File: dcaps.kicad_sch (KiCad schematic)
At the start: 1 part, among them U1 AM6254ATCGHAALW

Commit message: commit++
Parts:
- removed U1: AM6254ATCGHAALW, pepy_sym_lib:[CPU]Texas Instruments AM6254ATCGHAALW, symbol pepy_sym_lib:[CPU]Texas Instruments AM6254ATCGHAALW
- added C10, C11, C12, C13, C15, C16, C17, C8, C9: CL03A105MQ3CSNH, pepy_sym_lib:[CAP_SMD_0201_0603Metric], symbol pepy_sym_lib:[CAP_SMD_0201_0603Metric]Samsung Electro-Mechanics CL03A105MQ3CSNH
- added U1: AM6254ATCGHAALW, pepy_sym_lib:[CPU]Texas Instruments AM6254ATCGHAALW, symbol pepy_sym_lib:[CPU]Texas Instruments AM6254ATCGHAALW
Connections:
- new net: C9.2, U1.H11 (CAP_VDDS_MCU)
- new net: C15.2, U1.H15 (CAP_VDDS0)
- new net: C10.2, U1.J19 (CAP_VDDS6)
- new net: C17.2, U1.W17 (CAP_VDDS2)
- new net: C16.2, U1.K18 (CAP_VDDS1)
- new net: C12.2, U1.U7 (CAP_VDDS4)
- new net: C13.2, U1.H17 (CAP_VDDS5)
- new net: C8.2, U1.G9 (CAP_VDDS_CANUART)
- new net: C11.2, U1.P19 (CAP_VDDS3)
- new net GND: C10.1, C11.1, C12.1, C13.1, C15.1, C16.1, C17.1, C8.1, C9.1, U1.A1 (VSS), U1.A24 (VSS), U1.A25 (VSS), U1.AA11 (VSS), U1.AB9 (VSS), U1.AD1 (VSS), U1.AD12 (VSS), U1.AD16 (VSS), U1.AD25 (VSS), U1.AD9 (VSS), U1.AE1 (VSS), U1.AE12 (VSS), U1.AE16 (VSS), U1.AE24 (VSS), U1.AE25 (VSS), U1.AE8 (VSS), U1.B25 (VSS), U1.F13 (VSS), U1.G13 (VSS), U1.G19 (VSS), U1.H13 (VSS), U1.H16 (VSS), U1.H18 (VSS), U1.H20 (VSS), U1.J13 (VSS), U1.J7 (VSS), U1.K13 (VSS), U1.K15 (VSS), U1.K19 (VSS), U1.K7 (VSS), U1.L20 (VSS), U1.M10 (VSS), U1.M12 (VSS), U1.M13 (VSS), U1.M17 (VSS), U1.M18 (VSS), U1.M7 (VSS), U1.M8 (VSS), U1.N15 (VSS), U1.P10 (VSS), U1.P13 (VSS), U1.P7 (VSS), U1.R13 (VSS), U1.R15 (VSS), U1.R18 (VSS), U1.R20 (VSS), U1.T13 (VSS), U1.T14 (VSS), U1.T16 (VSS), U1.T17 (VSS), U1.T18 (VSS), U1.T8 (VSS), U1.U19 (VSS), U1.U8 (VSS), U1.V10 (VSS), U1.V11 (VSS), U1.V13 (VSS), U1.V16 (VSS), U1.V18 (VSS), U1.V9 (VSS), U1.W7 (VSS), U1.Y2 (VSS)

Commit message: PMIC draft
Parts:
- added C37: CL03A105MQ3CSNH, pepy_sym_lib:[CAP_SMD_0201_0603Metric], symbol pepy_sym_lib:[CAP_SMD_0201_0603Metric]Samsung Electro-Mechanics CL03A105MQ3CSNH
- added C38, C39, C40, C41, C42, C43, C44, C45, C46, C47, C48, C49, C50, C51, C52, C53: CC0201KRX5R6BB104, pepy_sym_lib:[CAP_SMD_0201_0603Metric], symbol pepy_sym_lib:[CAP_SMD_0201_0603Metric]YAGEO CC0201KRX5R6BB104
- added C54: CL05A475KP5NRNC, pepy_sym_lib:[CAP_SMD_0402_1005Metric], symbol pepy_sym_lib:[CAP_SMD_0402_1005Metric]Samsung Electro-Mechanics CL05A475KP5NRNC
- added C55: CC0402MRX5R5BB106, pepy_sym_lib:[CAP_SMD_0402_1005Metric], symbol pepy_sym_lib:[CAP_SMD_0402_1005Metric]YAGEO CC0402MRX5R5BB106
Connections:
- net GND: now also C37.1, C38.1, C39.1, C40.1, C41.1, C42.1, C43.1, C44.1, C45.1, C46.1, C47.1, C48.1, C49.1, C50.1, C51.1, C52.1, C53.1, C54.1, C55.1
- new net VDD_CORE: C37.2, C38.2, C39.2, C40.2, C41.2, C42.2, C43.2, C44.2, C45.2, C46.2, C47.2, C48.2, C49.2, C50.2, C51.2, C52.2, C53.2, C54.2, C55.2

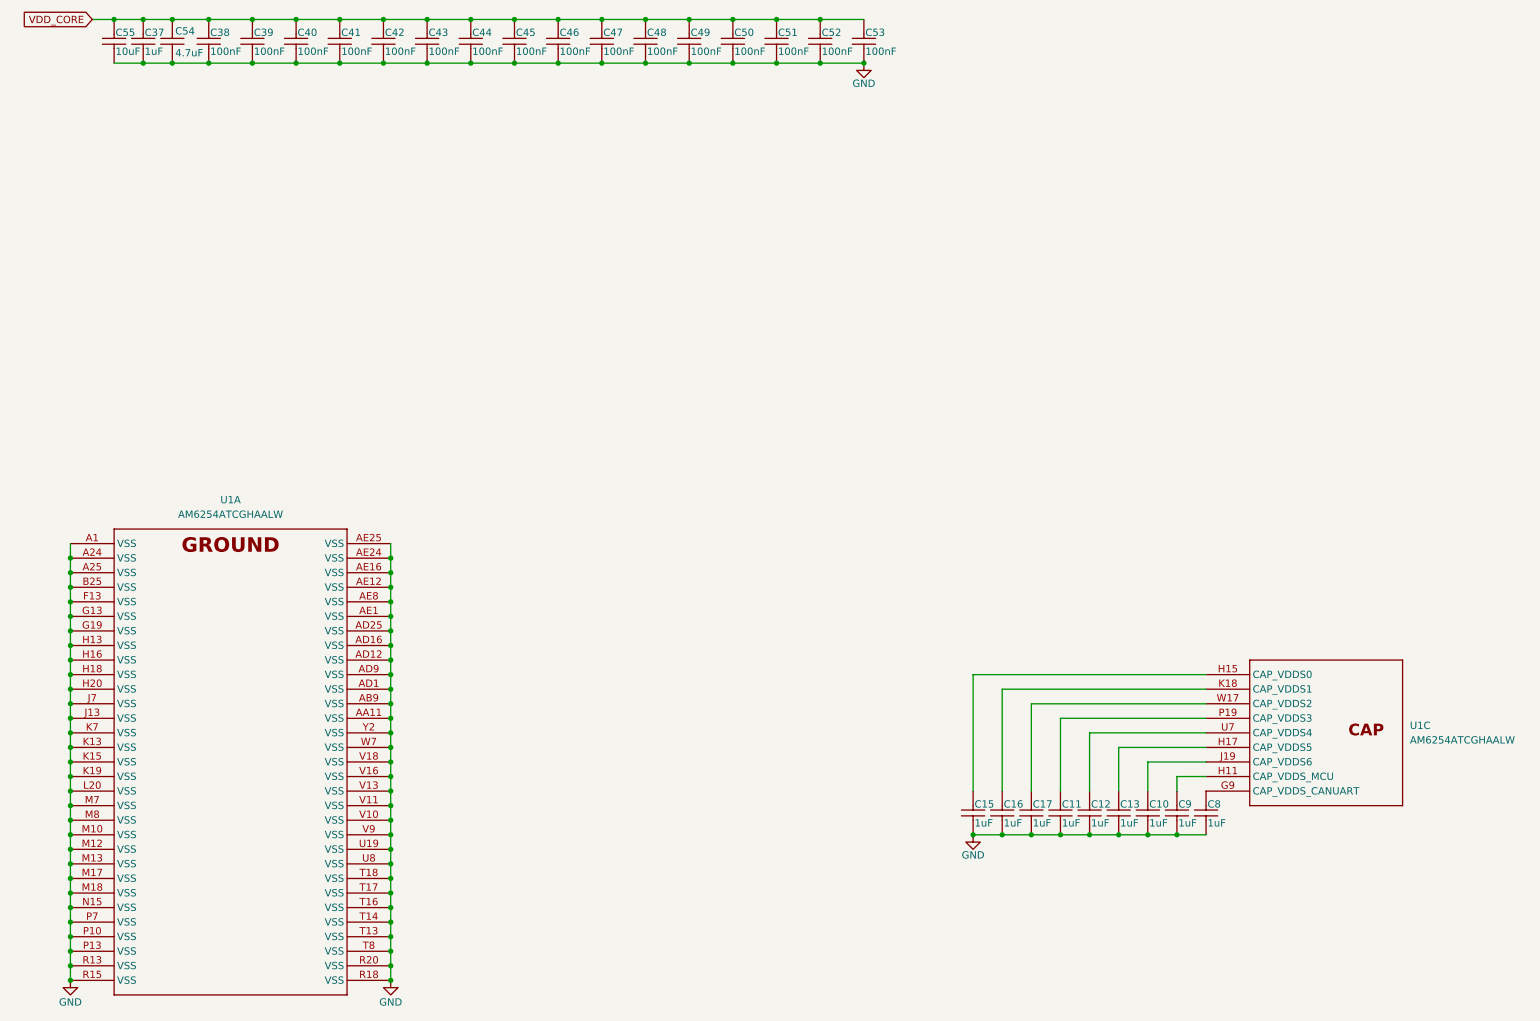
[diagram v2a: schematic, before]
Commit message: SD card changes
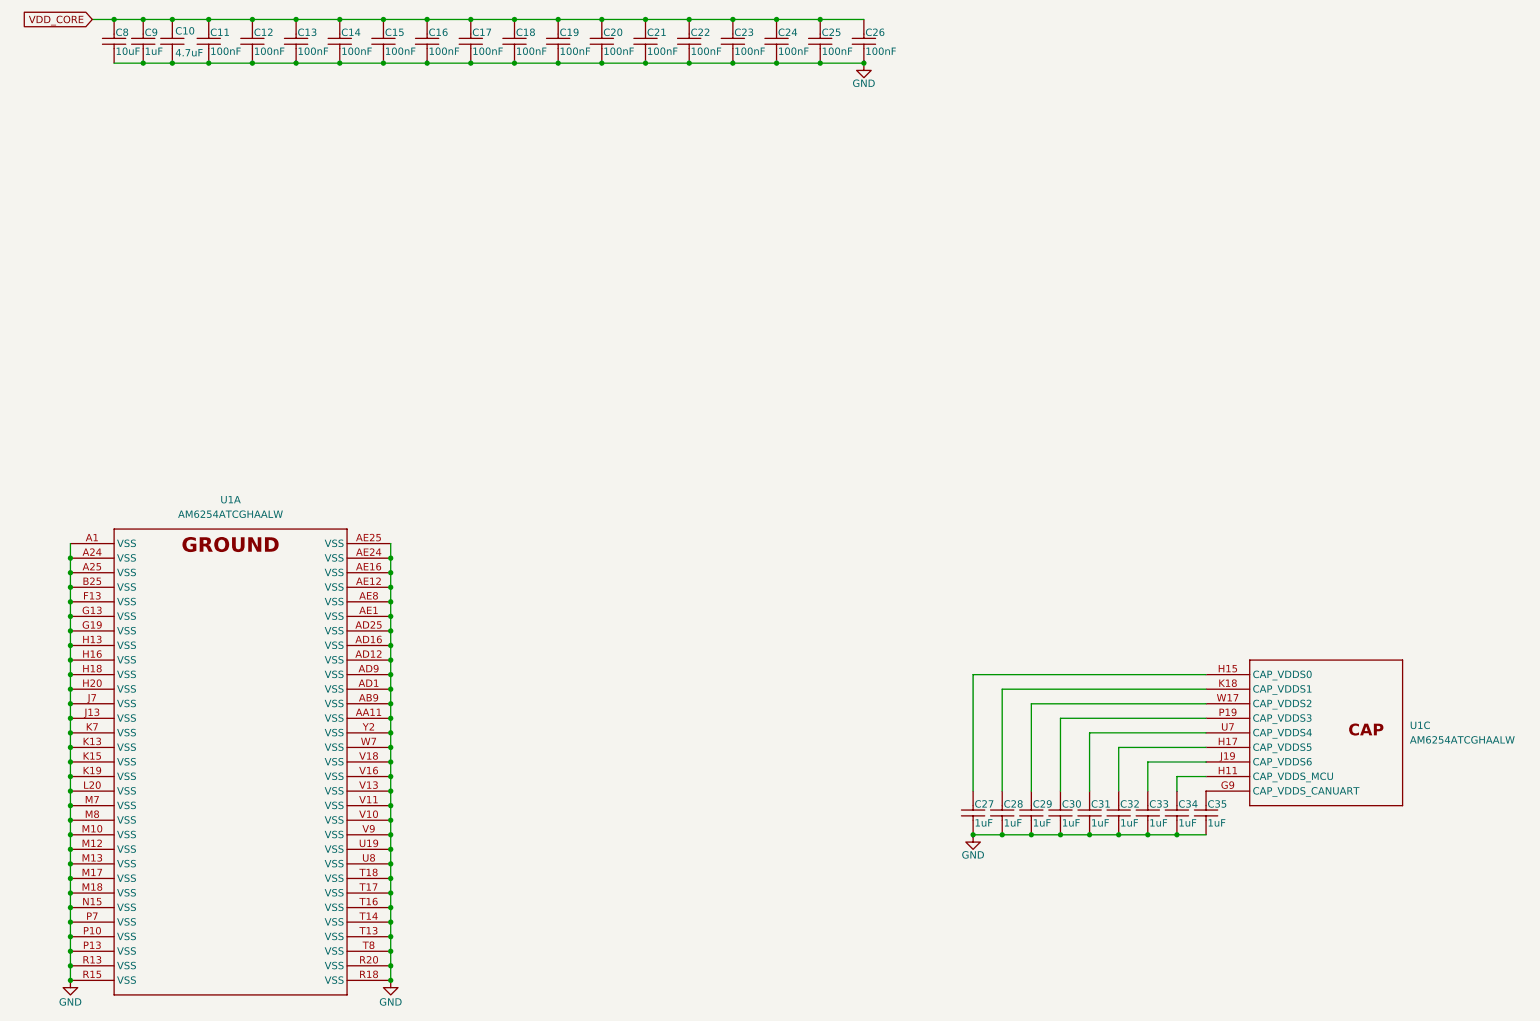
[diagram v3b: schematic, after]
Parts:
- renumbered C54 to C10, C38 to C11, C39 to C12, C40 to C13, C41 to C14, C42 to C15, C43 to C16, C44 to C17, C45 to C18, C46 to C19, C47 to C20, C48 to C21, C49 to C22, C50 to C23, C51 to C24, C52 to C25, C53 to C26, C15 to C27, C16 to C28, C17 to C29, C11 to C30, C12 to C31, C13 to C32, C10 to C33, C9 to C34, C8 to C35, C55 to C8, C37 to C9
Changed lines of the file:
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@@
 		(on_board yes)
 		(dnp no)
-		(property "Reference" "C9"
+		(property "Reference" "C34"
 			(at 217.424 154.686 90)
 			(effects
@@
 			(project "dashcam"
 				(path "/30d6913c-7aa4-4f56-9882-2ba08f7e2cce/97d97b12-d924-4e04-8775-cfa0a0f27f6a"
-					(reference "C9")
+					(reference "C34")
 					(unit 1)
 				)
@@
 		(on_board yes)
 		(dnp no)
-		(property "Reference" "C44"
+		(property "Reference" "C17"
 			(at 94.234 20.066 90)
 			(effects
@@
 			(project "dashcam"
 				(path "/30d6913c-7aa4-4f56-9882-2ba08f7e2cce/97d97b12-d924-4e04-8775-cfa0a0f27f6a"
-					(reference "C44")
+					(reference "C17")
 					(unit 1)
 				)
@@
 		(on_board yes)
 		(dnp no)
-		(property "Reference" "C52"
+		(property "Reference" "C25"
 			(at 155.194 20.066 90)
 			(effects
@@
 			(project "dashcam"
 				(path "/30d6913c-7aa4-4f56-9882-2ba08f7e2cce/97d97b12-d924-4e04-8775-cfa0a0f27f6a"
-					(reference "C52")
+					(reference "C25")
 					(unit 1)
 				)
@@
 		(on_board yes)
 		(dnp no)
-		(property "Reference" "C43"
+		(property "Reference" "C16"
 			(at 86.614 20.066 90)
 			(effects
@@
 			(project "dashcam"
 				(path "/30d6913c-7aa4-4f56-9882-2ba08f7e2cce/97d97b12-d924-4e04-8775-cfa0a0f27f6a"
-					(reference "C43")
+					(reference "C16")
 					(unit 1)
 				)
@@
 		(on_board yes)
 		(dnp no)
-		(property "Reference" "C15"
+		(property "Reference" "C27"
 			(at 181.864 154.686 90)
 			(effects
@@
 			(project "dashcam"
 				(path "/30d6913c-7aa4-4f56-9882-2ba08f7e2cce/97d97b12-d924-4e04-8775-cfa0a0f27f6a"
-					(reference "C15")
+					(reference "C27")
 					(unit 1)
 				)
@@
 		(on_board yes)
 		(dnp no)
-		(property "Reference" "#PWR053"
+		(property "Reference" "#PWR020"
 			(at 162.56 31.75 0)
 			(effects
@@
 			(project ""
 				(path "/30d6913c-7aa4-4f56-9882-2ba08f7e2cce/97d97b12-d924-4e04-8775-cfa0a0f27f6a"
-					(reference "#PWR053")
+					(reference "#PWR020")
 					(unit 1)
 				)
@@
 		(on_board yes)
 		(dnp no)
-		(property "Reference" "C38"
+		(property "Reference" "C11"
 			(at 48.514 20.066 90)
 			(effects
@@
 			(project ""
 				(path "/30d6913c-7aa4-4f56-9882-2ba08f7e2cce/97d97b12-d924-4e04-8775-cfa0a0f27f6a"
-					(reference "C38")
+					(reference "C11")
 					(unit 1)
 				)
@@
 		(on_board yes)
 		(dnp no)
-		(property "Reference" "C46"
+		(property "Reference" "C19"
 			(at 109.474 20.066 90)
 			(effects
@@
 			(project "dashcam"
 				(path "/30d6913c-7aa4-4f56-9882-2ba08f7e2cce/97d97b12-d924-4e04-8775-cfa0a0f27f6a"
-					(reference "C46")
+					(reference "C19")
 					(unit 1)
 				)
@@
 		(on_board yes)
 		(dnp no)
-		(property "Reference" "#PWR020"
+		(property "Reference" "#PWR018"
 			(at 24.13 191.77 0)
 			(effects
@@
 			(project "dashcam"
 				(path "/30d6913c-7aa4-4f56-9882-2ba08f7e2cce/97d97b12-d924-4e04-8775-cfa0a0f27f6a"
-					(reference "#PWR020")
+					(reference "#PWR018")
 					(unit 1)
 				)
@@
 		(on_board yes)
 		(dnp no)
-		(property "Reference" "C50"
+		(property "Reference" "C23"
 			(at 139.954 20.066 90)
 			(effects
@@
 			(project "dashcam"
 				(path "/30d6913c-7aa4-4f56-9882-2ba08f7e2cce/97d97b12-d924-4e04-8775-cfa0a0f27f6a"
-					(reference "C50")
+					(reference "C23")
 					(unit 1)
 				)
@@
 		(on_board yes)
 		(dnp no)
-		(property "Reference" "C53"
+		(property "Reference" "C26"
 			(at 162.814 20.066 90)
 			(effects
@@
 			(project "dashcam"
 				(path "/30d6913c-7aa4-4f56-9882-2ba08f7e2cce/97d97b12-d924-4e04-8775-cfa0a0f27f6a"
-					(reference "C53")
+					(reference "C26")
 					(unit 1)
 				)
@@
 		(on_board yes)
 		(dnp no)
-		(property "Reference" "C48"
+		(property "Reference" "C21"
 			(at 124.714 20.066 90)
 			(effects
@@
 			(project "dashcam"
 				(path "/30d6913c-7aa4-4f56-9882-2ba08f7e2cce/97d97b12-d924-4e04-8775-cfa0a0f27f6a"
-					(reference "C48")
+					(reference "C21")
 					(unit 1)
 				)
@@
 		(on_board yes)
 		(dnp no)
-		(property "Reference" "C37"
+		(property "Reference" "C9"
 			(at 37.084 20.066 90)
 			(effects
@@
 			(project "dashcam"
 				(path "/30d6913c-7aa4-4f56-9882-2ba08f7e2cce/97d97b12-d924-4e04-8775-cfa0a0f27f6a"
-					(reference "C37")
+					(reference "C9")
 					(unit 1)
 				)
@@
 		(on_board yes)
 		(dnp no)
-		(property "Reference" "C55"
+		(property "Reference" "C8"
 			(at 32.004 20.066 90)
 			(effects
@@
 			(project ""
 				(path "/30d6913c-7aa4-4f56-9882-2ba08f7e2cce/97d97b12-d924-4e04-8775-cfa0a0f27f6a"
-					(reference "C55")
+					(reference "C8")
 					(unit 1)
 				)
@@
 		(on_board yes)
 		(dnp no)
-		(property "Reference" "C49"
+		(property "Reference" "C22"
 			(at 132.334 20.066 90)
 			(effects
@@
 			(project "dashcam"
 				(path "/30d6913c-7aa4-4f56-9882-2ba08f7e2cce/97d97b12-d924-4e04-8775-cfa0a0f27f6a"
-					(reference "C49")
+					(reference "C22")
 					(unit 1)
 				)
@@
 		(on_board yes)
 		(dnp no)
-		(property "Reference" "C10"
+		(property "Reference" "C33"
 			(at 212.344 154.686 90)
 			(effects
@@
 			(project "dashcam"
 				(path "/30d6913c-7aa4-4f56-9882-2ba08f7e2cce/97d97b12-d924-4e04-8775-cfa0a0f27f6a"
-					(reference "C10")
+					(reference "C33")
 					(unit 1)
 				)
@@
 		(on_board yes)
 		(dnp no)
-		(property "Reference" "C45"
+		(property "Reference" "C18"
 			(at 101.854 20.066 90)
 			(effects
@@
 			(project "dashcam"
 				(path "/30d6913c-7aa4-4f56-9882-2ba08f7e2cce/97d97b12-d924-4e04-8775-cfa0a0f27f6a"
-					(reference "C45")
+					(reference "C18")
 					(unit 1)
 				)
@@
 		(on_board yes)
 		(dnp no)
-		(property "Reference" "C41"
+		(property "Reference" "C14"
 			(at 71.374 20.066 90)
 			(effects
@@
 			(project "dashcam"
 				(path "/30d6913c-7aa4-4f56-9882-2ba08f7e2cce/97d97b12-d924-4e04-8775-cfa0a0f27f6a"
-					(reference "C41")
+					(reference "C14")
 					(unit 1)
 				)
@@
 		(on_board yes)
 		(dnp no)
-		(property "Reference" "C42"
+		(property "Reference" "C15"
 			(at 78.994 20.066 90)
 			(effects
@@
 			(project "dashcam"
 				(path "/30d6913c-7aa4-4f56-9882-2ba08f7e2cce/97d97b12-d924-4e04-8775-cfa0a0f27f6a"
-					(reference "C42")
+					(reference "C15")
 					(unit 1)
 				)
@@
 		(on_board yes)
 		(dnp no)
-		(property "Reference" "C17"
+		(property "Reference" "C29"
 			(at 192.024 154.686 90)
 			(effects
@@
 			(project "dashcam"
 				(path "/30d6913c-7aa4-4f56-9882-2ba08f7e2cce/97d97b12-d924-4e04-8775-cfa0a0f27f6a"
-					(reference "C17")
+					(reference "C29")
 					(unit 1)
 				)
@@
 		(on_board yes)
 		(dnp no)
-		(property "Reference" "C39"
+		(property "Reference" "C12"
 			(at 56.134 20.066 90)
 			(effects
@@
 			(project "dashcam"
 				(path "/30d6913c-7aa4-4f56-9882-2ba08f7e2cce/97d97b12-d924-4e04-8775-cfa0a0f27f6a"
-					(reference "C39")
+					(reference "C12")
 					(unit 1)
 				)
@@
 		(on_board yes)
 		(dnp no)
-		(property "Reference" "C51"
+		(property "Reference" "C24"
 			(at 147.574 20.066 90)
 			(effects
@@
 			(project "dashcam"
 				(path "/30d6913c-7aa4-4f56-9882-2ba08f7e2cce/97d97b12-d924-4e04-8775-cfa0a0f27f6a"
-					(reference "C51")
+					(reference "C24")
 					(unit 1)
 				)
@@
 		(on_board yes)
 		(dnp no)
-		(property "Reference" "#PWR018"
+		(property "Reference" "#PWR021"
 			(at 181.61 166.37 0)
 			(effects
@@
 			(project "dashcam"
 				(path "/30d6913c-7aa4-4f56-9882-2ba08f7e2cce/97d97b12-d924-4e04-8775-cfa0a0f27f6a"
-					(reference "#PWR018")
+					(reference "#PWR021")
 					(unit 1)
 				)
@@
 		(on_board yes)
 		(dnp no)
-		(property "Reference" "C47"
+		(property "Reference" "C20"
 			(at 117.094 20.066 90)
 			(effects
@@
 			(project "dashcam"
 				(path "/30d6913c-7aa4-4f56-9882-2ba08f7e2cce/97d97b12-d924-4e04-8775-cfa0a0f27f6a"
-					(reference "C47")
+					(reference "C20")
 					(unit 1)
 				)
@@
 		(on_board yes)
 		(dnp no)
-		(property "Reference" "C40"
+		(property "Reference" "C13"
 			(at 63.754 20.066 90)
 			(effects
@@
 			(project "dashcam"
 				(path "/30d6913c-7aa4-4f56-9882-2ba08f7e2cce/97d97b12-d924-4e04-8775-cfa0a0f27f6a"
-					(reference "C40")
+					(reference "C13")
 					(unit 1)
 				)
@@
 		(on_board yes)
 		(dnp no)
-		(property "Reference" "C16"
+		(property "Reference" "C28"
 			(at 186.944 154.686 90)
 			(effects
@@
 			(project "dashcam"
 				(path "/30d6913c-7aa4-4f56-9882-2ba08f7e2cce/97d97b12-d924-4e04-8775-cfa0a0f27f6a"
-					(reference "C16")
+					(reference "C28")
 					(unit 1)
 				)
@@
 		(on_board yes)
 		(dnp no)
-		(property "Reference" "C12"
+		(property "Reference" "C31"
 			(at 202.184 154.686 90)
 			(effects
@@
 			(project "dashcam"
 				(path "/30d6913c-7aa4-4f56-9882-2ba08f7e2cce/97d97b12-d924-4e04-8775-cfa0a0f27f6a"
-					(reference "C12")
+					(reference "C31")
 					(unit 1)
 				)
@@
 		(on_board yes)
 		(dnp no)
-		(property "Reference" "C13"
+		(property "Reference" "C32"
 			(at 207.264 154.686 90)
 			(effects
@@
 			(project "dashcam"
 				(path "/30d6913c-7aa4-4f56-9882-2ba08f7e2cce/97d97b12-d924-4e04-8775-cfa0a0f27f6a"
-					(reference "C13")
+					(reference "C32")
 					(unit 1)
 				)
@@
 		(on_board yes)
 		(dnp no)
-		(property "Reference" "C54"
+		(property "Reference" "C10"
 			(at 42.418 19.812 90)
 			(effects
@@
 			(project ""
 				(path "/30d6913c-7aa4-4f56-9882-2ba08f7e2cce/97d97b12-d924-4e04-8775-cfa0a0f27f6a"
-					(reference "C54")
+					(reference "C10")
 					(unit 1)
 				)
@@
 		(on_board yes)
 		(dnp no)
-		(property "Reference" "C8"
+		(property "Reference" "C35"
 			(at 222.504 154.686 90)
 			(effects
@@
 			(project "dashcam"
 				(path "/30d6913c-7aa4-4f56-9882-2ba08f7e2cce/97d97b12-d924-4e04-8775-cfa0a0f27f6a"
-					(reference "C8")
+					(reference "C35")
 					(unit 1)
 				)
@@
 		(on_board yes)
 		(dnp no)
-		(property "Reference" "C11"
+		(property "Reference" "C30"
 			(at 197.104 154.686 90)
 			(effects
@@
 			(project "dashcam"
 				(path "/30d6913c-7aa4-4f56-9882-2ba08f7e2cce/97d97b12-d924-4e04-8775-cfa0a0f27f6a"
-					(reference "C11")
+					(reference "C30")
 					(unit 1)
 				)
